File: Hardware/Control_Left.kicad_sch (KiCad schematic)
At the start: 31 parts, among them J1 BAT, J2 TagConnect, J3 0.96_TFT_MODULE, Q1 AO3401A, Q2 AO3401A, SW1 MSK12C02, SW2 SW_Push, SW3 MSK12C02, U1 XIAO-NRF52840-PLUS, U2 TPS61040DBV

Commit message: MIP display and LED enable
Return of the LED enable via GPIO.
Changed the TFT display for a MPI panel. It's more expensive than an e-ink one, but the sharpness is really nice.
Need to remove the numbers row to go for a true Corne-ish layout.
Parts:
- removed D3: DSK24, Diode_SMD:D_SOD-123F, symbol Device:D_Schottky
- removed J3: 0.96_TFT_MODULE, Custom_Parts:0.96_TFT_MODULE, symbol Custom_Parts:0.96_TFT_MODULE
- removed Q2: AO3401A, Package_TO_SOT_SMD:SOT-23, symbol Transistor_FET:AO3401A
- removed R1: 100K, Resistor_SMD:R_0603_1608Metric, symbol Device:R
- removed R10, R9: 10K, Resistor_SMD:R_0603_1608Metric, symbol Device:R
- removed R11: 22, Resistor_SMD:R_0603_1608Metric, symbol Device:R
- removed R8: 100, Resistor_SMD:R_0603_1608Metric, symbol Device:R
- removed SW3: MSK12C02, Custom_Parts:MSK12C02, symbol Custom_Parts:MSK12C02
- removed U2: TPS61040DBV, Package_TO_SOT_SMD:SOT-23-5, symbol Regulator_Switching:TPS61040DBV
- added C7: 1u, Capacitor_SMD:C_0603_1608Metric, symbol Device:C
- added FB1, FB2: 600, Inductor_SMD:L_0603_1608Metric, symbol Device:FerriteBead
- added J3: 1.08_MIP_MODULE, Custom_Parts:1.08_MIP_MODULE, symbol Custom_Parts:1.08_MIP_MODULE
- added R2: 100K, Resistor_SMD:R_0603_1608Metric, symbol Device:R
- added R5: 150K, Resistor_SMD:R_0603_1608Metric, symbol Device:R
- added U1: TPS61040DBV, Package_TO_SOT_SMD:SOT-23-5, symbol Regulator_Switching:TPS61040DBV
- C6: value 1u -> 1n; JLC Part C15849 -> C1588; Manufacturer Part CL10A105KB8NNNC -> CL10B102KB8NNNC
- R3: value 470K -> 10K; JLC Part C23178 -> 0603WAF1002T5E; Manufacturer Part 0603WAF4703T5E -> 0603WAF1002T5E
- R4: value 150K -> 470K; JLC Part C22807 -> C23178; Manufacturer Part 0603WAF1503T5E -> 0603WAF4703T5E
- renumbered R2 to R1, R5 to R6, R6 to R7, R7 to R8, U1 to U2
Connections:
- net VCOM is gone; now on net VREGL: D1.1 (K), Q1.2 (S)
- net 3V3L: now also C7.1, FB1.1, J3.7 (VDD); no longer C6.1
- net 5VL: now also R4.1; no longer R3.1
- net GND: now also R3.1, C7.2, FB2.1, J3.4 (EXTCOM), J3.8 (EXTMOD), J3.9 (VSS), J3.MP, R2.2, R5.2, U1.2 (GND); no longer C5.2, R4.2
- net VBUSL: now also R2.1
- net VFB: now also R4.2, R5.1, U1.3 (FB); no longer R3.2, R4.1
- net VREGL: now also U1.5 (VIN)
- net VSW: now also U1.1 (SW)
- net LCD_BKL renamed MIP_EN
- net MIP_EN: now also C6.1, J3.5 (DISP)
- net LCD_CS renamed LED_EN
- net LED_EN: now also R3.2, U1.4 (EN)
- net LCD_DC renamed MIP_CS
- net MIP_CS: now also J3.3 (SCS)
- net LCD_MOSI renamed MIP_MOSI
- net MIP_MOSI: now also J3.2 (SI)
- net LCD_RES renamed MIP_VDDA
- net MIP_VDDA: now also FB1.2, J3.6 (VDDA)
- net LCD_SCK renamed MIP_SCK
- net MIP_SCK: now also J3.1 (SCLK)
- new net MIP_VSSA: C5.2, FB2.2, J3.10 (VSSA)
- no-connect marks 3 -> 2

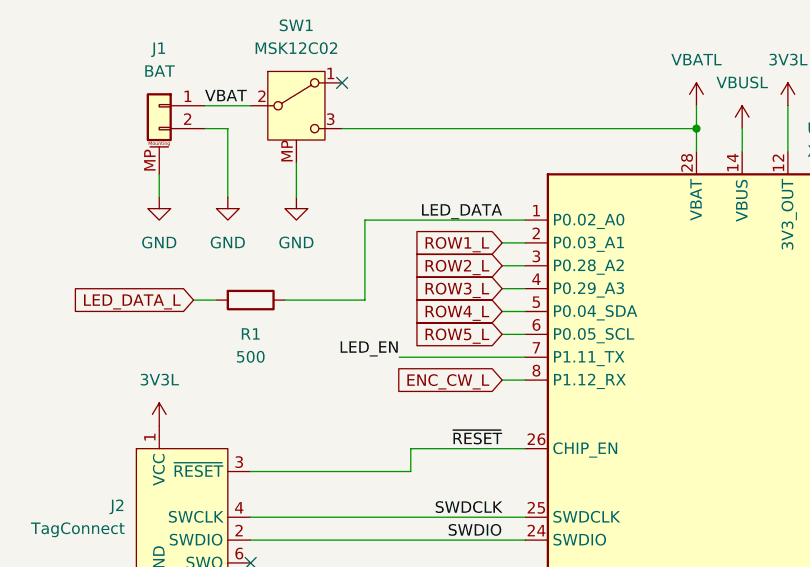
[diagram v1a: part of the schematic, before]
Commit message: Row removal and key layout
Removed the number row.
Adjusted the spacebar position and changed it to 1u.
Need to consider what to do for one of the halfs if its screen is to be removed.
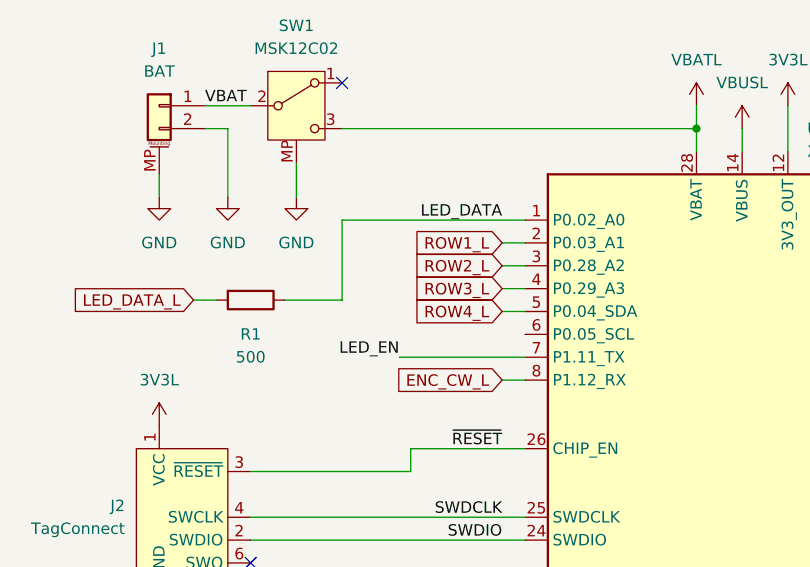
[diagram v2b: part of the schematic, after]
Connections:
- net ROW5_L: no longer names the net of U2.6 (P0.05_SCL)
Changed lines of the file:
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@@
 	(wire
 		(pts
-			(xy 72.39 53.34) (xy 90.17 53.34)
+			(xy 69.85 53.34) (xy 90.17 53.34)
 		)
 		(stroke
@@
 	(wire
 		(pts
-			(xy 72.39 62.23) (xy 72.39 53.34)
+			(xy 69.85 62.23) (xy 69.85 53.34)
 		)
 		(stroke
@@
 	(wire
 		(pts
-			(xy 63.5 62.23) (xy 72.39 62.23)
+			(xy 63.5 62.23) (xy 69.85 62.23)
 		)
 		(stroke
@@
 		(pts
 			(xy 193.04 106.68) (xy 193.04 121.92)
-		)
-		(stroke
-			(width 0)
-			(type default)
-		)
-	)
-	(wire
-		(pts
-			(xy 87.63 66.04) (xy 90.17 66.04)
 		)
 		(stroke
@@
 			)
 		)
-	)
-	(global_label "ROW5_L"
-		(shape input)
-		(at 87.63 66.04 180)
-		(fields_autoplaced yes)
-		(effects
-			(font
-				(size 1.27 1.27)
-			)
-			(justify right)
-		)
-		(property "Intersheetrefs" "${INTERSHEET_REFS}"
-			(at 77.811 66.04 0)
-			(hide yes)
-			(show_name no)
-			(do_not_autoplace no)
-			(effects
-				(font
-					(size 1.27 1.27)
-				)
-				(justify right)
-			)
-		)

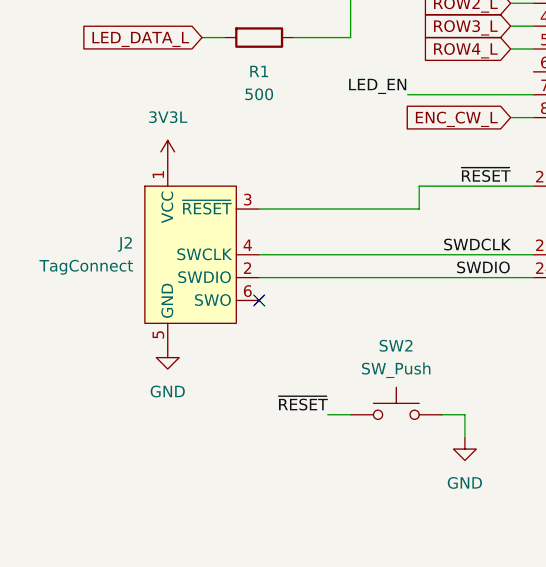
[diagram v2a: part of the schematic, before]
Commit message: Debug connector
Updated the debug connector for a custom one.
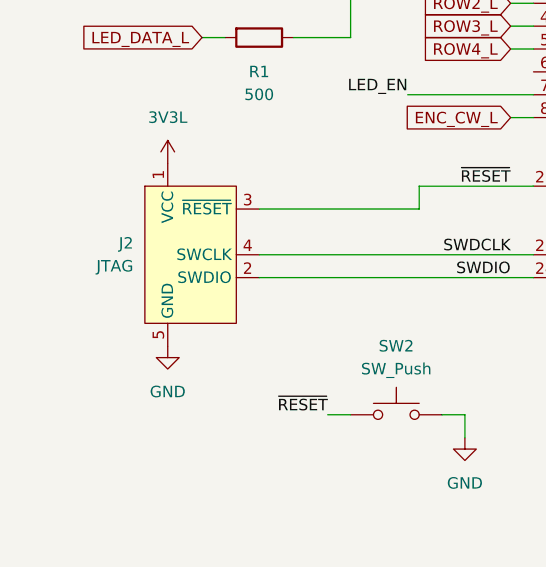
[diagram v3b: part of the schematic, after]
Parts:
- removed J2: TagConnect, Connector:Tag-Connect_TC2030-IDC-NL_2x03_P1.27mm_Vertical, symbol Connector:Conn_ARM_SWD_TagConnect_TC2030-NL
- added J2: JTAG, Custom_Parts:JTAG_SWD_1X05_1.27MM_COMBO, symbol Custom_Parts:JTAG_SWD_1X05_1.27MM_COMBO
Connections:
- net 3V3L: now also J2.1 (VCC)
- net GND: now also J2.5 (GND)
- net SWDCLK: now also J2.4 (SWCLK)
- net SWDIO: now also J2.2 (SWDIO)
- net ~{RESET}: now also J2.3 (~{RESET})
- no-connect marks 2 -> 1
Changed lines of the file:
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@@
 		(at 69.85 38.1)
 	)
-	(no_connect
-		(at 59.69 91.44)
-	)
 	(wire
 		(pts
@@
 	)
 	(symbol
+		(lib_id "Custom_Parts:JTAG_SWD_1X05_1.27MM_COMBO")
+		(at 52.07 86.36 0)
+		(unit 1)
+		(body_style 1)
+		(exclude_from_sim no)
+		(in_bom no)
+		(on_board yes)
+		(in_pos_files no)
+		(dnp no)
+		(fields_autoplaced yes)
+		(property "Reference" "J2"
+			(at 45.72 85.0899 0)
+			(show_name no)
+			(do_not_autoplace no)
+			(effects
+				(font
+					(size 1.27 1.27)
+				)
+				(justify right)
+			)
+		)
+		(property "Value" "JTAG"
+			(at 45.72 87.6299 0)
+			(show_name no)
+			(do_not_autoplace no)
+			(effects
+				(font
+					(size 1.27 1.27)
+				)
+				(justify right)
+			)
+		)
+		(property "Footprint" "Custom_Parts:JTAG_SWD_1X05_1.27MM_COMBO"
+			(at 52.07 104.14 0)
+			(hide yes)
+			(show_name no)
+			(do_not_autoplace no)
+			(effects
+				(font
+					(size 1.27 1.27)
+				)
+			)
+		)
+		(property "Datasheet" ""
+			(at 52.07 101.6 0)
+			(hide yes)
+			(show_name no)
+			(do_not_autoplace no)
+			(effects
+				(font
+					(size 1.27 1.27)
+				)
+			)
+		)
+		(property "Description" "Custom JTAG connector based on 1x05 pad footprint"
+			(at 52.07 86.36 0)
+			(hide yes)
+			(show_name no)
+			(do_not_autoplace no)
+			(effects
+				(font
+					(size 1.27 1.27)
+				)
+			)
+		)
+		(property "JLC Part" "-"
+			(at 52.07 86.36 0)
+			(hide yes)
+			(show_name no)
+			(do_not_autoplace no)
+			(effects
+				(font
+					(size 1.27 1.27)
+				)
+			)
+		)
+		(property "Manufacturer Part" "-"
+			(at 52.07 86.36 0)
+			(hide yes)
+			(show_name no)
+			(do_not_autoplace no)
+			(effects
+				(font
+					(size 1.27 1.27)
+				)
+			)
+		)
+		(pin "5"
+		)
+		(pin "2"
+		)
+		(pin "3"
+		)
+		(pin "4"
+		)
+		(pin "1"
+		)
+		(instances
+			(project "ValkiriaSplit"
+				(path "/7a2b6783-81dc-46bd-bbde-89342e0b1c5b/5d937f2a-6ebc-416c-8541-68d6f5af5bcd"
+					(reference "J2")
+					(unit 1)
+				)
+			)
+		)
+	)
+	(symbol
 		(lib_id "power:+3V3")
 		(at 226.06 106.68 0)
@@
 					(unit 1)
 				)
-			)
-		)
-	)
-	(symbol
-		(lib_id "Connector:Conn_ARM_SWD_TagConnect_TC2030-NL")
-		(at 52.07 86.36 0)
-		(unit 1)
-		(body_style 1)
-		(exclude_from_sim no)
-		(in_bom no)
-		(on_board yes)
-		(in_pos_files no)
-		(dnp no)
-		(fields_autoplaced yes)
-		(property "Reference" "J2"
-			(at 45.72 85.0899 0)
-			(show_name no)
-			(do_not_autoplace no)
-			(effects
-				(font
-					(size 1.27 1.27)
-				)
-				(justify right)
-			)
-		)
-		(property "Value" "TagConnect"
-			(at 45.72 87.6299 0)
-			(show_name no)
-			(do_not_autoplace no)
-			(effects
-				(font
-					(size 1.27 1.27)
-				)
-				(justify right)
-			)
-		)
-		(property "Footprint" "Connector:Tag-Connect_TC2030-IDC-NL_2x03_P1.27mm_Vertical"
-			(at 52.07 104.14 0)
-			(hide yes)
-			(show_name no)
-			(do_not_autoplace no)
-			(effects
-				(font
-					(size 1.27 1.27)
-				)
-			)
-		)
-		(property "Datasheet" "https://www.tag-connect.com/wp-content/uploads/bsk-pdf-manager/TC2030-CTX_1.pdf"
-			(at 52.07 101.6 0)
-			(hide yes)
-			(show_name no)
-			(do_not_autoplace no)
-			(effects
-				(font
-					(size 1.27 1.27)
-				)
-			)
-		)
-		(property "Description" "Tag-Connect ARM Cortex SWD JTAG connector, 6 pin, no legs"
-			(at 52.07 86.36 0)
-			(hide yes)
-			(show_name no)
-			(do_not_autoplace no)
-			(effects
-				(font
-					(size 1.27 1.27)
-				)
-			)
-		)
-		(property "JLC Part" "-"
-			(at 52.07 86.36 0)
-			(hide yes)
-			(show_name no)
-			(do_not_autoplace no)
-			(effects
-				(font
-					(size 1.27 1.27)
-				)
-			)
-		)
-		(property "Manufacturer Part" "-"
-			(at 52.07 86.36 0)
-			(hide yes)
-			(show_name no)
-			(do_not_autoplace no)
-			(effects
-				(font
-					(size 1.27 1.27)
-				)
-			)
-		)
-		(pin "2"
-		)
-		(pin "4"
-		)
-		(pin "3"
-		)
-		(pin "1"
-		)
-		(pin "5"
-		)
-		(pin "6"
-		)
-		(instances
-			(project "ValkiriaSplit"
-				(path "/7a2b6783-81dc-46bd-bbde-89342e0b1c5b/5d937f2a-6ebc-416c-8541-68d6f5af5bcd"
-					(reference "J2")
-					(unit 1)
-				)

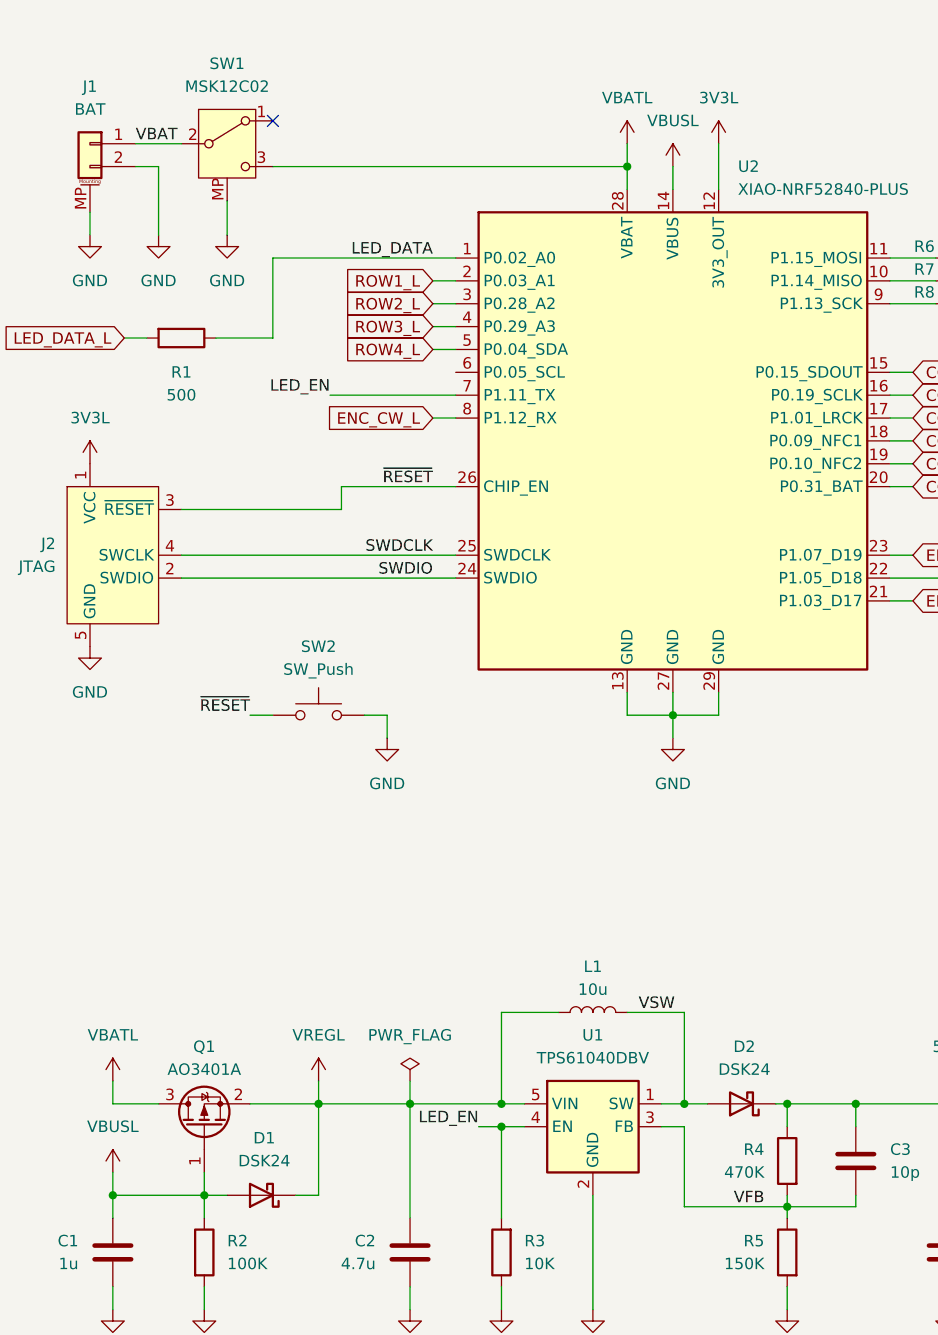
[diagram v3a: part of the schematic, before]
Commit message: Board outline and routing
Enlarged the board outline by 0.5mm for proper fitment of the switch receptacles.
Updated the footprint for the switch receptacles.
Changed the JTAG connector for a custom one.
Need to review the size of the PCB area dedicated to the MCU and the screen.
Need to consider removing the additional reset button.
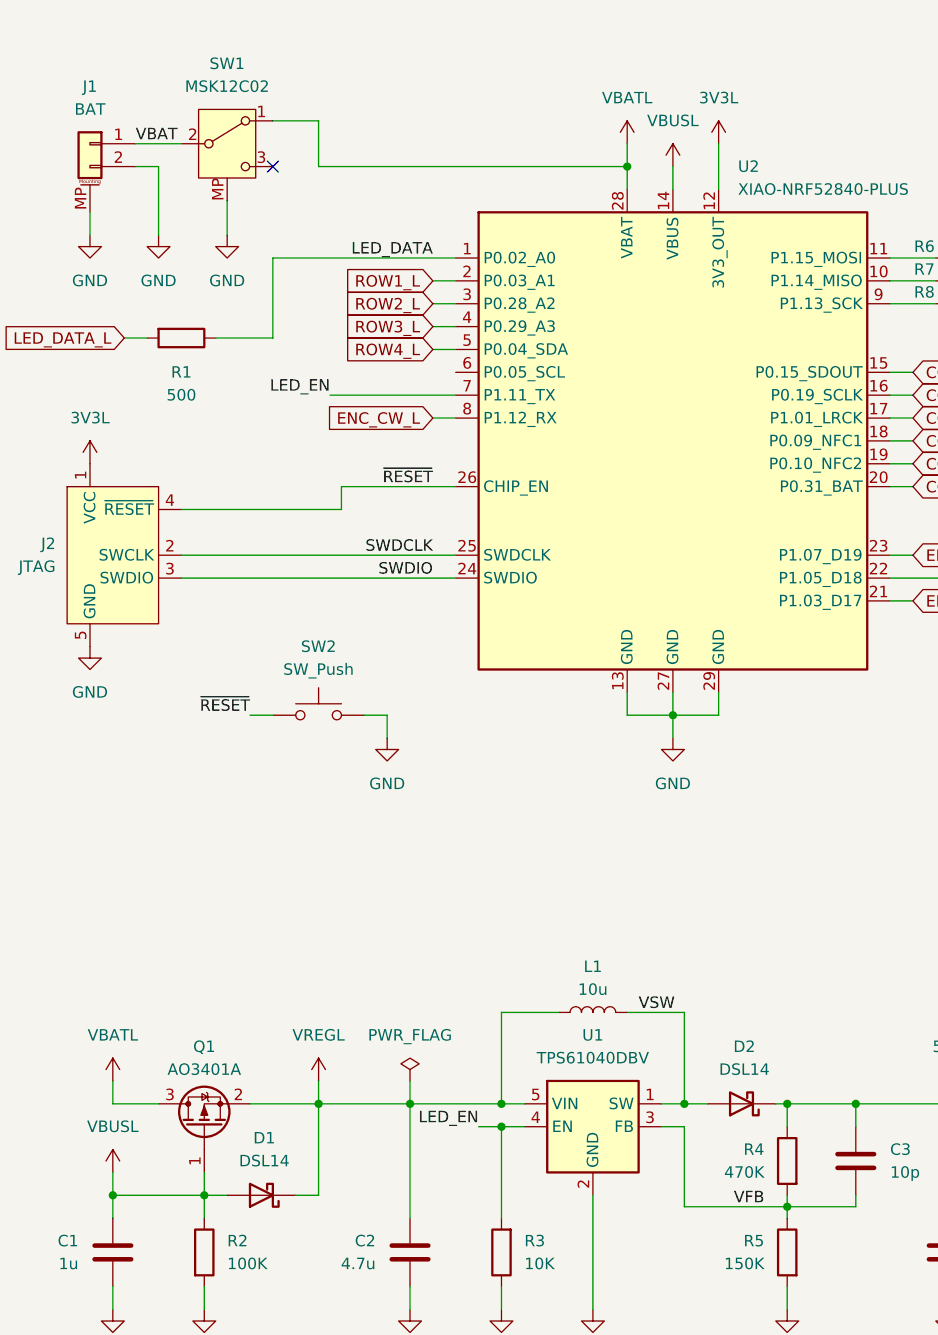
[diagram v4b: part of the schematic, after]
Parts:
- D1, D2: value DSK24 -> DSL14; JLC Part C22466352 -> C22466349; Manufacturer Part DSK24 -> DSL14
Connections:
- net SWDCLK: now also J2.2 (SWCLK); no longer J2.4 (SWCLK)
- net SWDIO: now also J2.3 (SWDIO); no longer J2.2 (SWDIO)
- net VBATL: now also SW1.1 (A); no longer SW1.3 (C)
- net ~{RESET}: now also J2.4 (~{RESET}); no longer J2.3 (~{RESET})
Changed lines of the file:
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@@
 	)
 	(junction
-		(at 109.22 43.18)
-		(diameter 0)
-		(color 0 0 0 0)
-	)
-	(junction
 		(at 127 158.75)
 		(diameter 0)
@@
 	)
 	(junction
+		(at 109.22 43.18)
+		(diameter 0)
+		(color 0 0 0 0)
+	)
+	(junction
 		(at 85.09 147.32)
 		(diameter 0)
@@
 	)
 	(no_connect
-		(at 69.85 38.1)
+		(at 69.85 43.18)
 	)
 	(wire
@@
 	(wire
 		(pts
-			(xy 109.22 40.64) (xy 109.22 43.18)
-		)
-		(stroke
-			(width 0)
-			(type default)
-		)
-	)
-	(wire
-		(pts
 			(xy 213.36 121.92) (xy 213.36 123.19)
 		)
@@
 	(wire
 		(pts
-			(xy 109.22 43.18) (xy 109.22 45.72)
+			(xy 109.22 40.64) (xy 109.22 43.18)
 		)
 		(stroke
@@
 	(wire
 		(pts
+			(xy 74.93 43.18) (xy 109.22 43.18)
+		)
+		(stroke
+			(width 0)
+			(type default)
+		)
+	)
+	(wire
+		(pts
 			(xy 219.71 119.38) (xy 219.71 133.35)
 		)
@@
 	(wire
 		(pts
+			(xy 74.93 38.1) (xy 74.93 43.18)
+		)
+		(stroke
+			(width 0)
+			(type default)
+		)
+	)
+	(wire
+		(pts
 			(xy 138.43 58.42) (xy 143.51 58.42)
 		)
@@
 	(wire
 		(pts
-			(xy 69.85 43.18) (xy 109.22 43.18)
-		)
-		(stroke
-			(width 0)
-			(type default)
-		)
-	)
-	(wire
-		(pts
 			(xy 232.41 116.84) (xy 232.41 127)
 		)
@@
 	(wire
 		(pts
+			(xy 69.85 38.1) (xy 74.93 38.1)
+		)
+		(stroke
+			(width 0)
+			(type default)
+		)
+	)
+	(wire
+		(pts
 			(xy 138.43 78.74) (xy 140.97 78.74)
 		)
@@
 	(wire
 		(pts
+			(xy 109.22 43.18) (xy 109.22 45.72)
+		)
+		(stroke
+			(width 0)
+			(type default)
+		)
+	)
+	(wire
+		(pts
 			(xy 226.06 140.97) (xy 226.06 142.24)
 		)
@@
 		(pin "2"
 		)
-		(pin "3"
-		)
 		(pin "4"
 		)
+		(pin "3"
+		)
 		(pin "1"
 		)
@@
 			)
 		)
-		(property "Value" "DSK24"
+		(property "Value" "DSL14"
 			(at 122.2375 143.51 0)
 			(show_name no)
@@
 			)
 		)
-		(property "JLC Part" "C22466352"
+		(property "JLC Part" "C22466349"
 			(at 121.92 147.32 0)
 			(hide yes)
@@
 			)
 		)
-		(property "Manufacturer Part" "DSK24"
+		(property "Manufacturer Part" "DSL14"
 			(at 121.92 147.32 0)
 			(hide yes)
@@
 			)
 		)
-		(property "Value" "DSK24"
+		(property "Value" "DSL14"
 			(at 68.8975 153.67 0)
 			(show_name no)
@@
 			)
 		)
-		(property "JLC Part" "C22466352"
+		(property "JLC Part" "C22466349"
 			(at 68.58 157.48 0)
 			(hide yes)
@@
 			)
 		)
-		(property "Manufacturer Part" "DSK24"
+		(property "Manufacturer Part" "DSL14"
 			(at 68.58 157.48 0)
 			(hide yes)
